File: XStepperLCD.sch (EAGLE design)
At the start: 28 parts, among them Q2 16 MHZ, U1 LCD-16X2NOHOLES

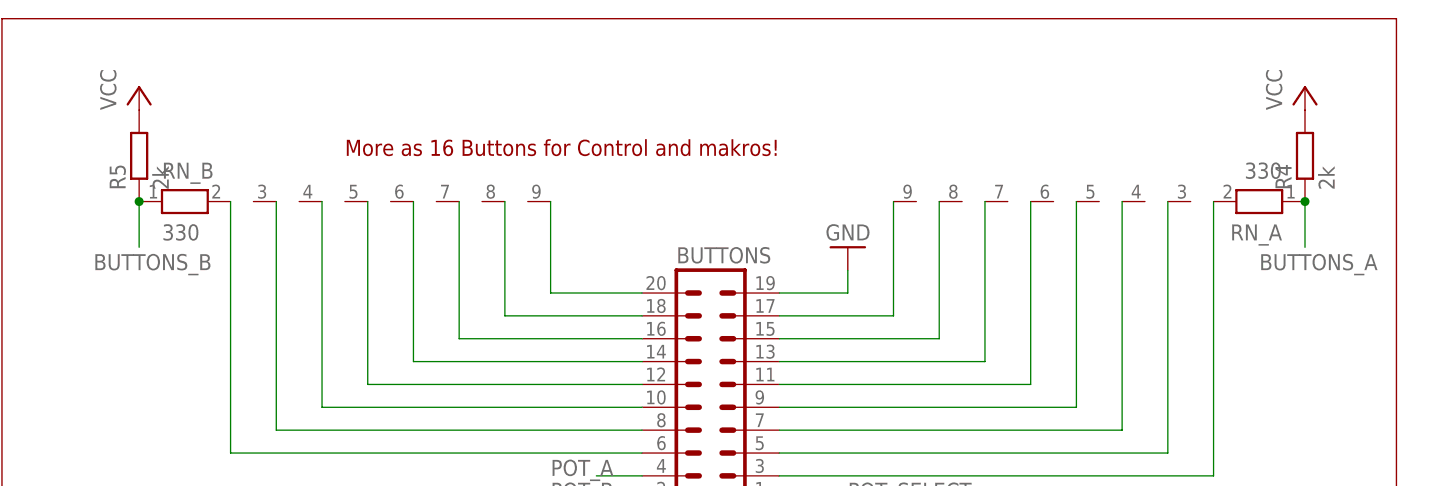
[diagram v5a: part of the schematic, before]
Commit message: - rename all mySerial to grblSerial
- add and use phi_interfaces for rotary encoder
- change intervall to 500ms and 1000ms for threads
- send reset if connected to grbl for UniversalGcodeSender
- add call_button
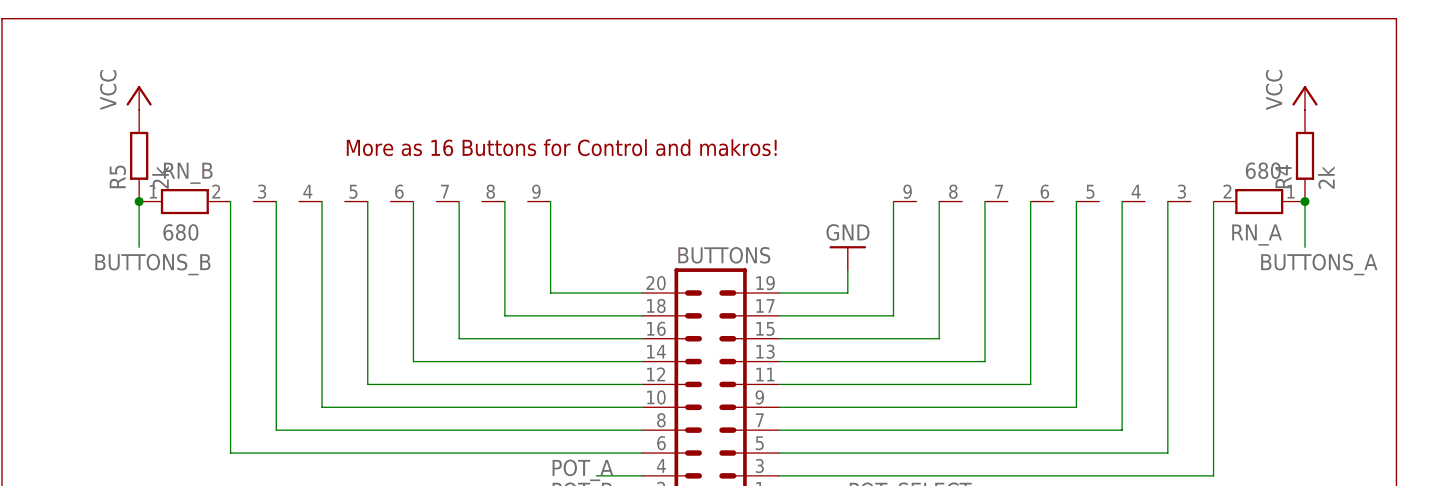
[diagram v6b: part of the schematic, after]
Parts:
- RN_A, RN_B: value 330 -> 680
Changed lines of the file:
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@@
 <grid distance="0.1" unitdist="inch" unit="inch" style="lines" multiple="1" display="no" altdistance="0.01" altunitdist="inch" altunit="inch"/>
 <layers>
-<layer number="1" name="Top" color="4" fill="1" visible="yes" active="no"/>
-<layer number="16" name="Bottom" color="1" fill="1" visible="yes" active="no"/>
-<layer number="17" name="Pads" color="2" fill="1" visible="yes" active="no"/>
-<layer number="18" name="Vias" color="2" fill="1" visible="yes" active="no"/>
-<layer number="19" name="Unrouted" color="6" fill="1" visible="yes" active="no"/>
-<layer number="20" name="Dimension" color="15" fill="1" visible="yes" active="no"/>
-<layer number="21" name="tPlace" color="7" fill="1" visible="yes" active="no"/>
-<layer number="22" name="bPlace" color="7" fill="1" visible="yes" active="no"/>
-<layer number="23" name="tOrigins" color="15" fill="1" visible="yes" active="no"/>
-<layer number="24" name="bOrigins" color="15" fill="1" visible="yes" active="no"/>
-<layer number="25" name="tNames" color="7" fill="1" visible="yes" active="no"/>
-<layer number="26" name="bNames" color="7" fill="1" visible="yes" active="no"/>
-<layer number="27" name="tValues" color="7" fill="1" visible="yes" active="no"/>
-<layer number="28" name="bValues" color="7" fill="1" visible="yes" active="no"/>
+<layer number="1" name="Top" color="4" fill="1" visible="no" active="no"/>
+<layer number="16" name="Bottom" color="1" fill="1" visible="no" active="no"/>
+<layer number="17" name="Pads" color="2" fill="1" visible="no" active="no"/>
+<layer number="18" name="Vias" color="2" fill="1" visible="no" active="no"/>
+<layer number="19" name="Unrouted" color="6" fill="1" visible="no" active="no"/>
+<layer number="20" name="Dimension" color="15" fill="1" visible="no" active="no"/>
+<layer number="21" name="tPlace" color="7" fill="1" visible="no" active="no"/>
+<layer number="22" name="bPlace" color="7" fill="1" visible="no" active="no"/>
+<layer number="23" name="tOrigins" color="15" fill="1" visible="no" active="no"/>
+<layer number="24" name="bOrigins" color="15" fill="1" visible="no" active="no"/>
+<layer number="25" name="tNames" color="7" fill="1" visible="no" active="no"/>
+<layer number="26" name="bNames" color="7" fill="1" visible="no" active="no"/>
+<layer number="27" name="tValues" color="7" fill="1" visible="no" active="no"/>
+<layer number="28" name="bValues" color="7" fill="1" visible="no" active="no"/>
 <layer number="29" name="tStop" color="7" fill="3" visible="no" active="no"/>
 <layer number="30" name="bStop" color="7" fill="6" visible="no" active="no"/>
@@
 <layer number="35" name="tGlue" color="7" fill="4" visible="no" active="no"/>
 <layer number="36" name="bGlue" color="7" fill="5" visible="no" active="no"/>
-<layer number="37" name="tTest" color="7" fill="1" visible="yes" active="no"/>
-<layer number="38" name="bTest" color="7" fill="1" visible="yes" active="no"/>
+<layer number="37" name="tTest" color="7" fill="1" visible="no" active="no"/>
+<layer number="38" name="bTest" color="7" fill="1" visible="no" active="no"/>
 <layer number="39" name="tKeepout" color="4" fill="11" visible="no" active="no"/>
 <layer number="40" name="bKeepout" color="1" fill="11" visible="no" active="no"/>
@@
 <layer number="44" name="Drills" color="7" fill="1" visible="no" active="no"/>
 <layer number="45" name="Holes" color="7" fill="1" visible="no" active="no"/>
-<layer number="46" name="Milling" color="3" fill="1" visible="yes" active="no"/>
-<layer number="47" name="Measures" color="7" fill="1" visible="yes" active="no"/>
-<layer number="48" name="Document" color="7" fill="1" visible="yes" active="no"/>
-<layer number="49" name="Reference" color="7" fill="1" visible="yes" active="no"/>
-<layer number="50" name="dxf" color="7" fill="1" visible="yes" active="no"/>
-<layer number="51" name="tDocu" color="7" fill="1" visible="yes" active="no"/>
-<layer number="52" name="bDocu" color="7" fill="1" visible="yes" active="no"/>
-<layer number="53" name="tGND_GNDA" color="7" fill="9" visible="yes" active="no"/>
-<layer number="54" name="bGND_GNDA" color="1" fill="9" visible="yes" active="no"/>
-<layer number="56" name="wert" color="7" fill="1" visible="yes" active="no"/>
+<layer number="46" name="Milling" color="3" fill="1" visible="no" active="no"/>
+<layer number="47" name="Measures" color="7" fill="1" visible="no" active="no"/>
+<layer number="48" name="Document" color="7" fill="1" visible="no" active="no"/>
+<layer number="49" name="Reference" color="7" fill="1" visible="no" active="no"/>
+<layer number="50" name="dxf" color="7" fill="1" visible="no" active="no"/>
+<layer number="51" name="tDocu" color="7" fill="1" visible="no" active="no"/>
+<layer number="52" name="bDocu" color="7" fill="1" visible="no" active="no"/>
+<layer number="53" name="tGND_GNDA" color="7" fill="9" visible="no" active="no"/>
+<layer number="54" name="bGND_GNDA" color="1" fill="9" visible="no" active="no"/>
+<layer number="56" name="wert" color="7" fill="1" visible="no" active="no"/>
 <layer number="91" name="Nets" color="2" fill="1" visible="yes" active="yes"/>
 <layer number="92" name="Busses" color="1" fill="1" visible="yes" active="yes"/>
@@
 <part name="P+1" library="supply1" deviceset="VCC" device=""/>
 <part name="BUTTONS" library="con-ml" deviceset="ML20" device=""/>
-<part name="RN_A" library="resistor-net" deviceset="RN08" device="" value="330"/>
+<part name="RN_A" library="resistor-net" deviceset="RN08" device="" value="680"/>
 <part name="P+9" library="supply1" deviceset="VCC" device=""/>
 <part name="R4" library="resistor" deviceset="R-EU_" device="0204/7" value="2k"/>
-<part name="RN_B" library="resistor-net" deviceset="RN08" device="" value="330"/>
+<part name="RN_B" library="resistor-net" deviceset="RN08" device="" value="680"/>
 <part name="P+7" library="supply1" deviceset="VCC" device=""/>
 <part name="R5" library="resistor" deviceset="R-EU_" device="0204/7" value="2k"/>

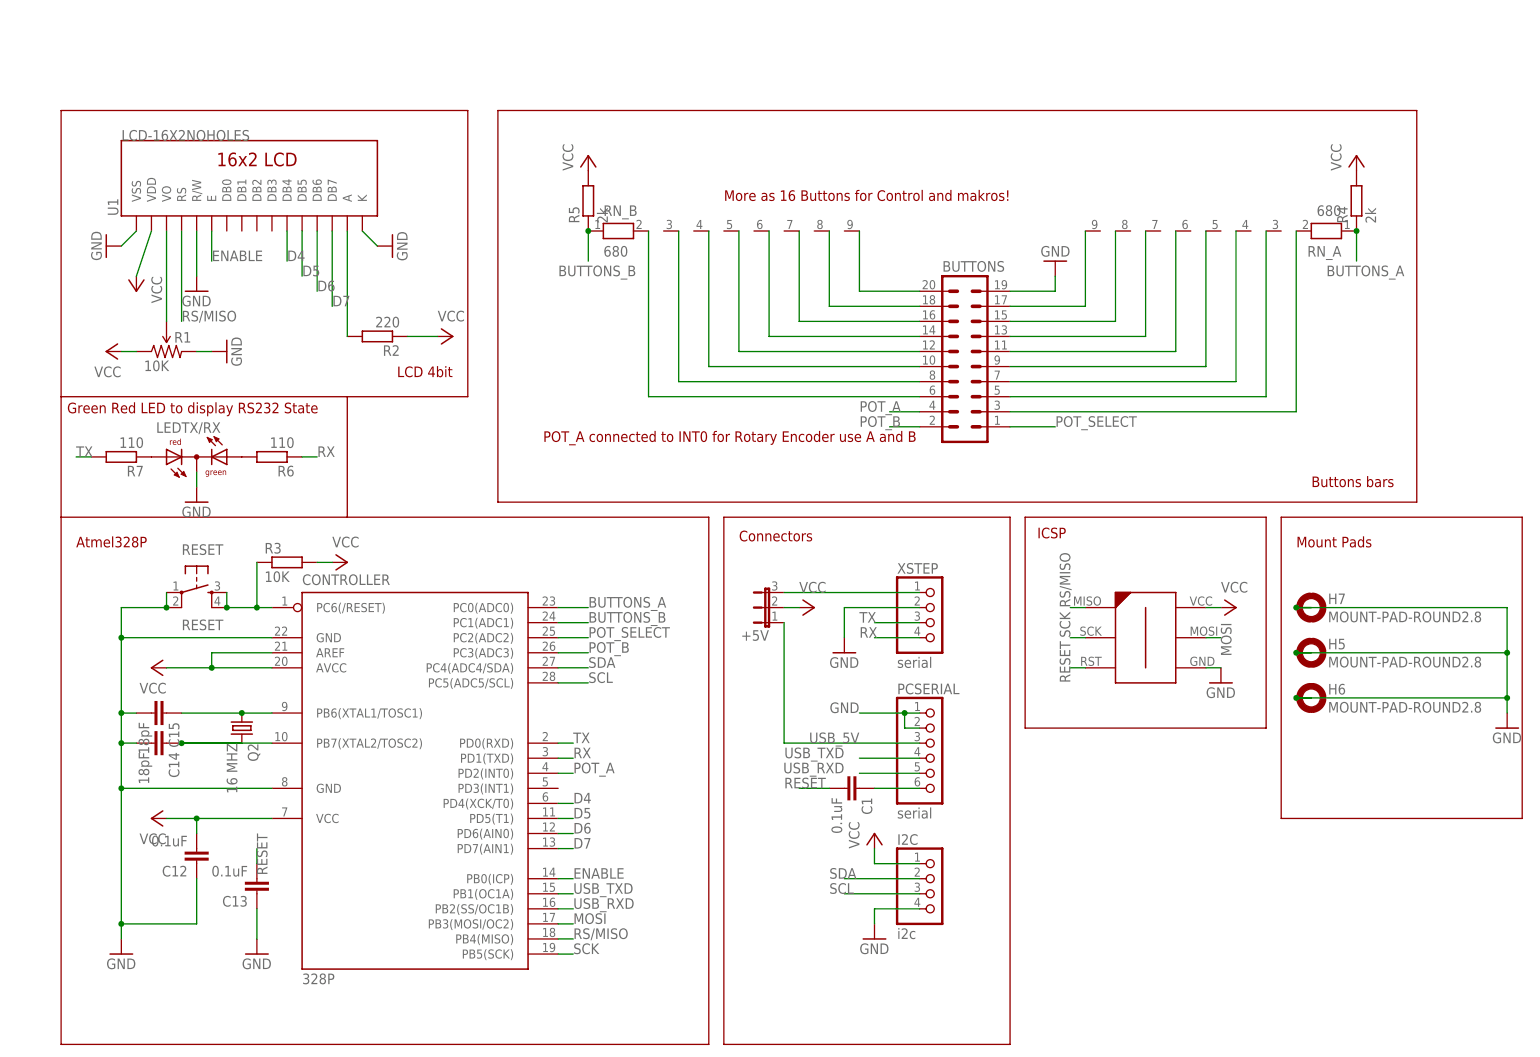
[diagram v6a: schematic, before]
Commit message: - change to 0.2 and produce pcb
- change all resistors and caps to SMD 1206
- change RX/TX Wires to USB_RXD/USB_TXD
- move RX/TX to Pin 14 and pin 15
- use Pin 4,5 for RotaryEncoder
- use POT_Select on Pin 16
- move Enable to mosi pin
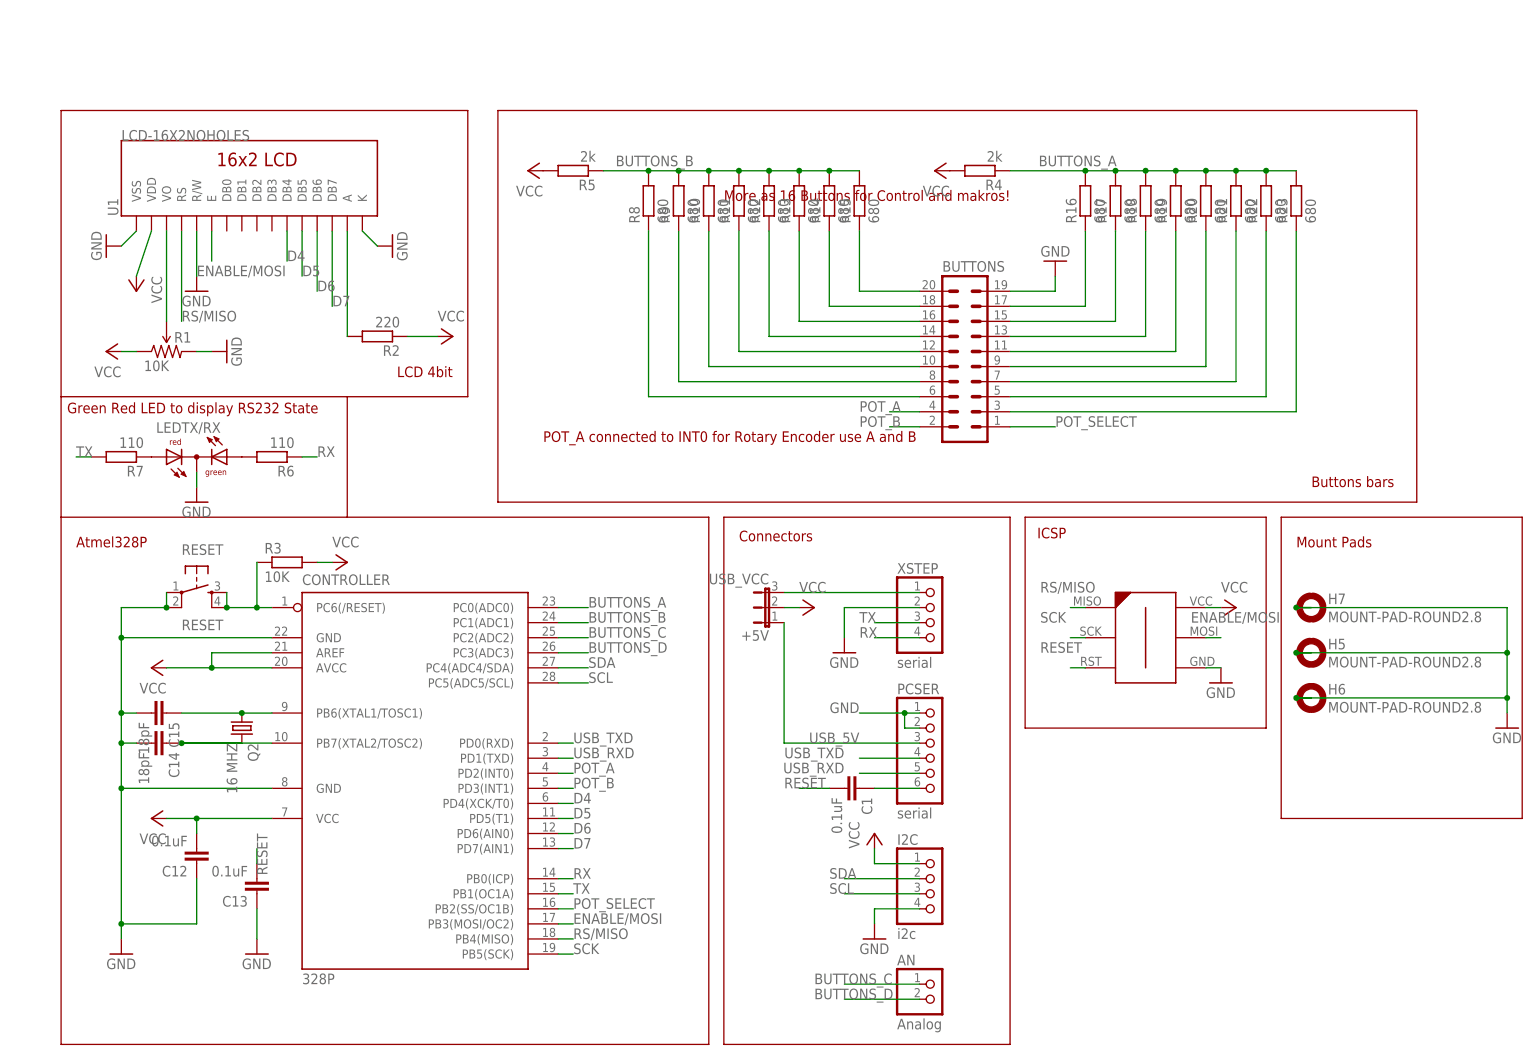
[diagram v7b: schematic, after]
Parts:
- removed RN_A, RN_B: 680, resistor-net:RN08
- added AN: Analog, pinhead:PINHD-1X2
- added R10, R11, R12, R13, R14, R15, R16, R17, R18, R19, R20, R21, R22, R23, R8, R9: 680, resistor:R-EU_R1206
- +5V: value (none) -> USB_VCC
- C1, C12, C13, C14, C15: device resistor:C-EU025-025X050 -> resistor:C-EUC1206
- R2, R3, R4, R5, R6, R7: device resistor:R-EU_0204/7 -> resistor:R-EU_R1206
- RESET: device SparkFun:TAC_SWITCHPTH -> SparkFun:TAC_SWITCHSMD
- renumbered PCSERIAL to PCSER
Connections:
- removed net ENABLE: 328P.PB0(ICP), U1.E
- removed net MOSI: 328P.PB3(MOSI/OC2), ICSP.P$5
- new net BUTTONS_C: 328P.PC2(ADC2), AN.1
- new net BUTTONS_D: 328P.PC3(ADC3), AN.2
- new net ENABLE/MOSI: 328P.PB3(MOSI/OC2), ICSP.P$5, U1.E
- net BUTTONS_A: now also R16.2, R17.2, R18.2, R19.2, R20.2, R21.2, R22.2, R23.2; no longer RN_A.1
- net BUTTONS_B: now also R10.2, R11.2, R12.2, R13.2, R14.2, R15.2, R8.2, R9.2; no longer RN_B.1
- net N$10: now also R22.1; no longer RN_A.3
- net N$11: now also R10.1; no longer RN_B.4
- net N$12: now also R11.1; no longer RN_B.5
- net N$13: now also R12.1; no longer RN_B.6
- net N$15: now also R13.1; no longer RN_B.7
- net N$16: now also R21.1; no longer RN_A.4
- net N$17: now also R20.1; no longer RN_A.5
- net N$18: now also R19.1; no longer RN_A.6
- net N$19: now also R14.1; no longer RN_B.8
- net N$20: now also R15.1; no longer RN_B.9
- net N$4: now also R18.1; no longer RN_A.7
- net N$5: now also R17.1; no longer RN_A.8
- net N$6: now also R16.1; no longer RN_A.9
- net N$7: now also R8.1; no longer RN_B.2
- net N$8: now also R9.1; no longer RN_B.3
- net N$9: now also R23.1; no longer RN_A.2
- net POT_B: now also 328P.PD3(INT1); no longer 328P.PC3(ADC3)
- net POT_SELECT: now also 328P.PB2(SS/OC1B); no longer 328P.PC2(ADC2)
- net RX: now also 328P.PB0(ICP); no longer 328P.PD1(TXD)
- net TX: now also 328P.PB1(OC1A); no longer 328P.PD0(RXD)
- net USB_RXD: now also 328P.PD1(TXD); no longer 328P.PB2(SS/OC1B)
- net USB_TXD: now also 328P.PD0(RXD); no longer 328P.PB1(OC1A)
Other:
- moved on the sheet: R4, R5
